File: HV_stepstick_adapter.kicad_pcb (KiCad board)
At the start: 2 copper layers, 16.2 x 48.9 mm, 5 parts, among them J1 Screw_Terminal_01x02, J2 Conn_01x08, J3 Conn_01x08, J4 Conn_01x02

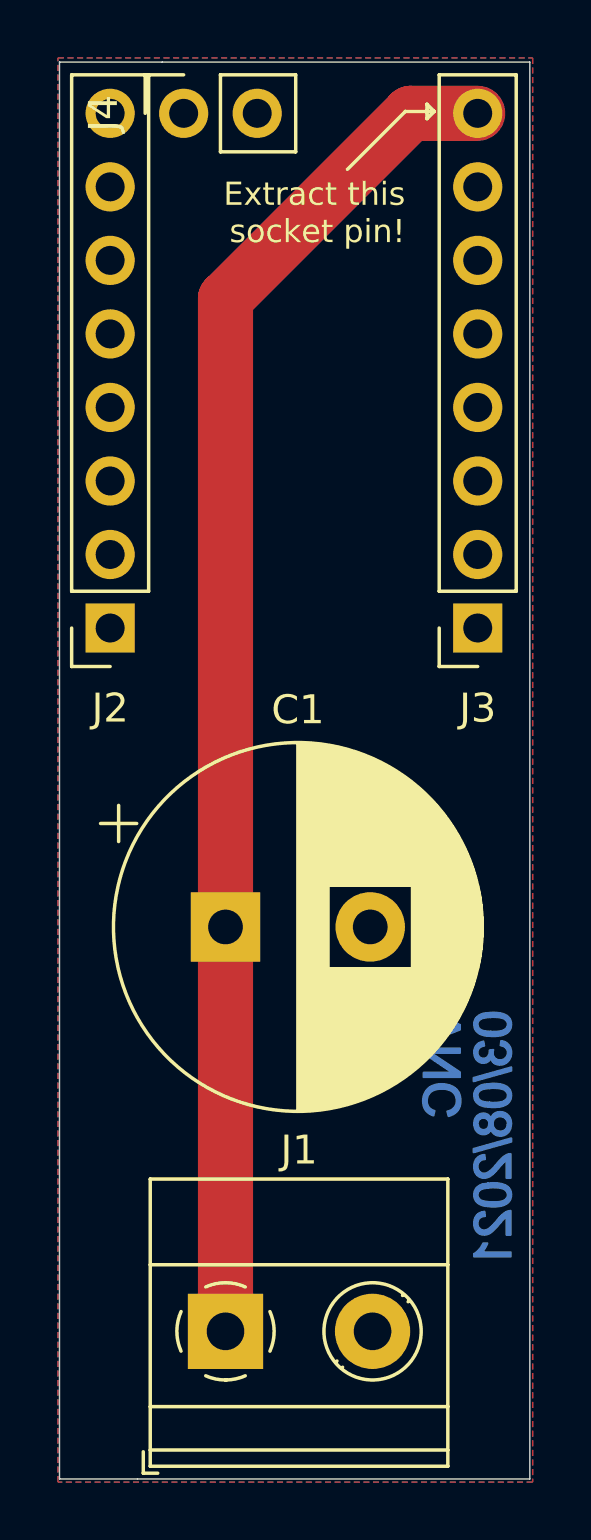
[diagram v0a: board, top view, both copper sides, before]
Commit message: Added diode for safety
Added a Schottky diode between VDD and VMOT lines for safety; also slightly reduced PCB width, to improve the fit on boards; and now Gerber files are available.
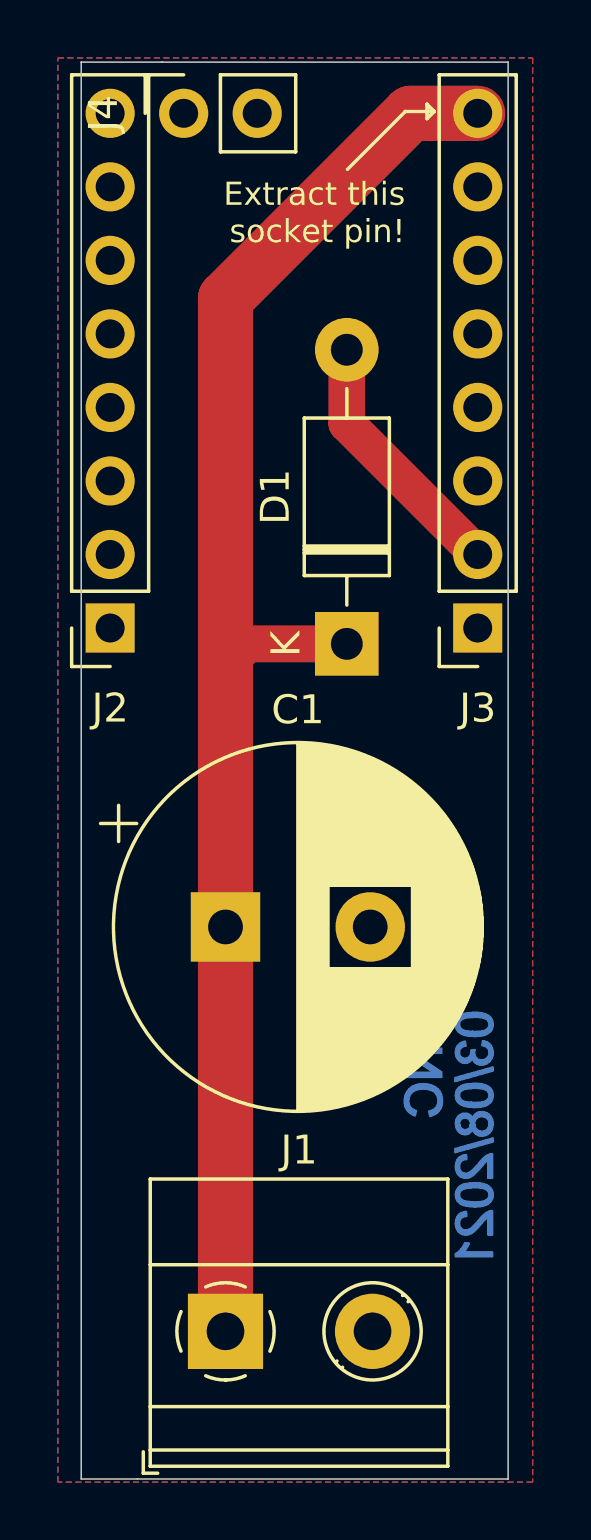
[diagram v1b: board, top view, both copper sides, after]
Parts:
- added D1: MBR1100G, Diode_THT:D_DO-41_SOD81_P10.16mm_Horizontal, F.Cu at (102.0, 128.1)
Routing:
- net VDD: track 0.00 -> 8.95 mm
- net VMOT: track 47.0 -> 51.6 mm
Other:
- board size 16.2 x 48.9 mm -> 14.7 x 48.9 mm
